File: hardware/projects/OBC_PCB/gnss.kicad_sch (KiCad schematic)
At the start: 15 parts, among them J8 RF coax pads, U1 MAX-F11N

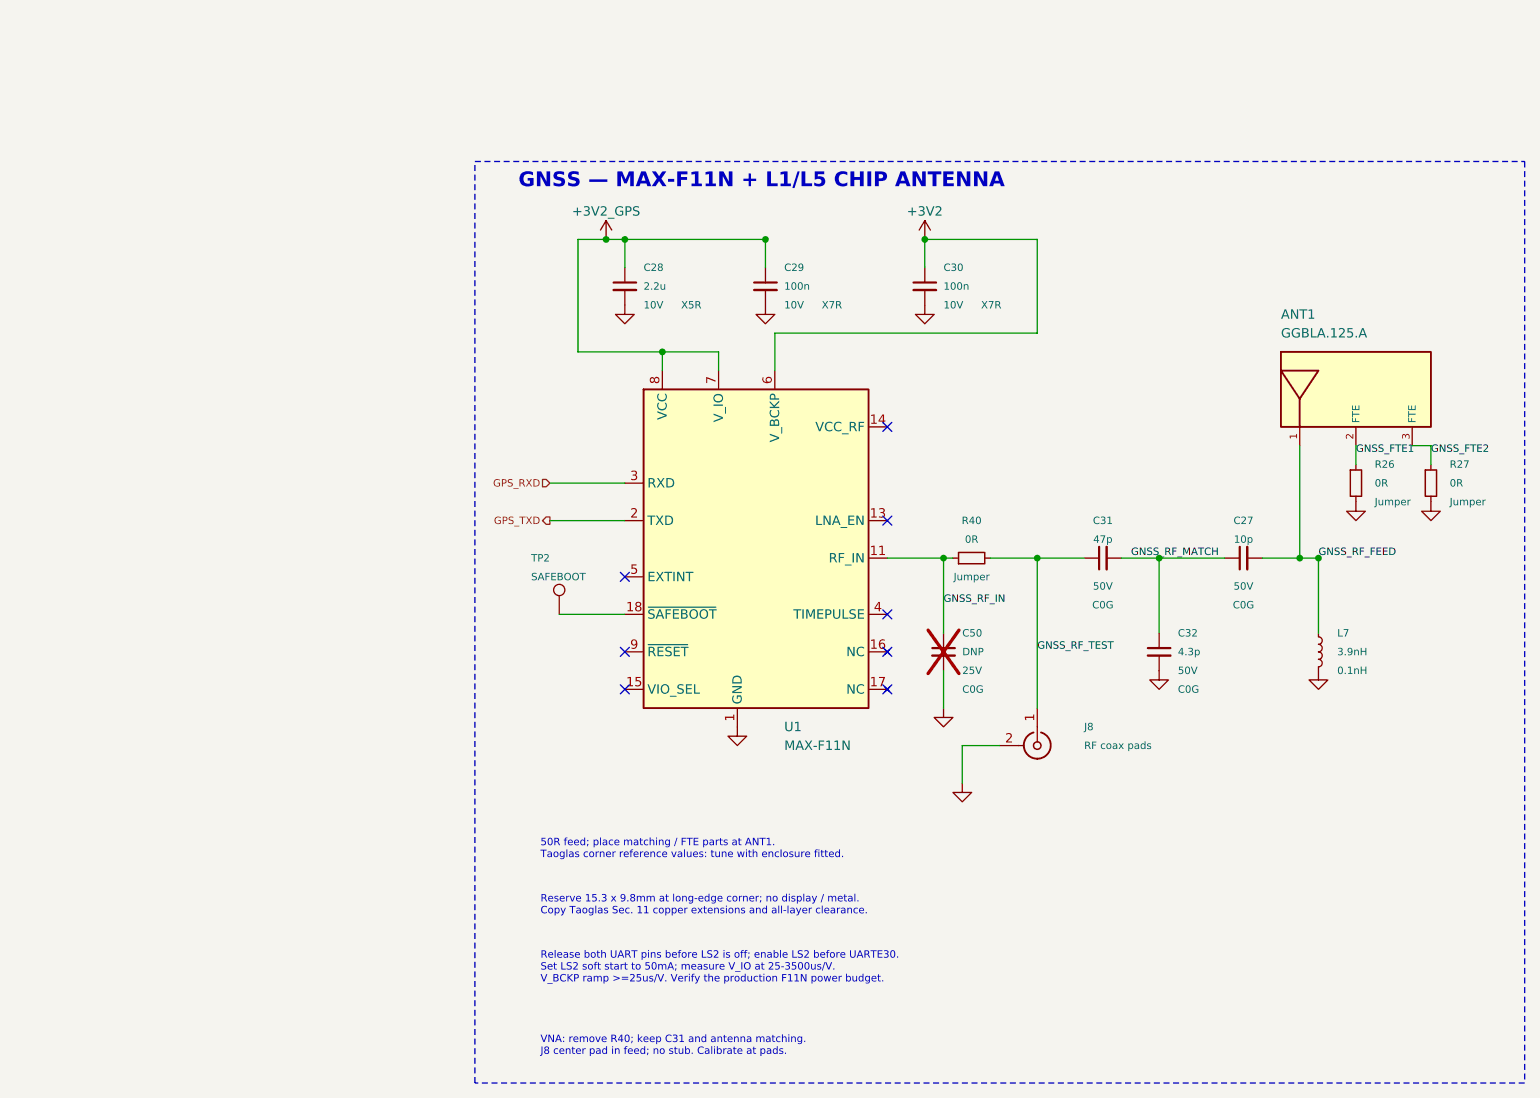
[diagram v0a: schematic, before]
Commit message: hardware: tidy the QFN schematic layout and style
Layout pass on the eight sheets. ERC stays at 0 violations on OBC_PCB and
USB_Baseboard. A netlist comparison shows the same 127 net partitions and
the same components, values and footprints.

Root sheet
- Draw SCL, SDA, COM_EN, LOUD, SHPHLD, BTN_SELECT and BUZZER_PWM as label
  stubs. Wire crossings fall from 38 to 0.
- Redraw the DCC/DECD/DECA/DECRF network as a chain without crossings.
- Move R5 and C26 clear of the crystal wires. Use a ground symbol on Y1
  instead of a label named GND.
- Hang the I2C test points on the U6C stubs.

Power sheet
- Attach the VBUS, VBAT and GND power flags to their nets.
- Tap TP1 onto the SHPHLD wire.
- Use a +3V2 symbol on LSIN2 instead of a label.
- Route SW2, the VSET straps and the CFG resistors without crossings.
- Move the SEL ground away from the LX1 pin.
- Show LSOUT1(GND) and INT(GND) for the unused LS1 and BMP581 pins.

Display, GNSS, user I/O
- Move J1 pin VA below VB so the VCOM/VB link no longer crosses VA.
- Move the GNSS FTE labels clear of the antenna pin 3 wire.
- Straighten the piezo wiring. Put the GND probe pad above its ground
  symbol.

Style
- One heading size (1.8 bold), one sub-heading size (1.27 bold) and one
  note size (1.0).
- Hide the voltage, dielectric and tolerance fields on the GNSS and radio
  sheets. Remove their dashed frames. Move both sheets to the top-left.
- Use Rev QFN and the same title format on every sheet.
- Set TP1 and TP2 to in_bom no like the other probe pads.
- Add C21 to the VDD bypass note.

Net names change for five nets because their labels are now on the root
sheet: BTN_SELECT, BUZZER_PWM, COM_EN, LOUD and SHPHLD. No net class
pattern uses them.

Co-Authored-By: Claude Sonnet 5.5 <noreply@anthropic.com>
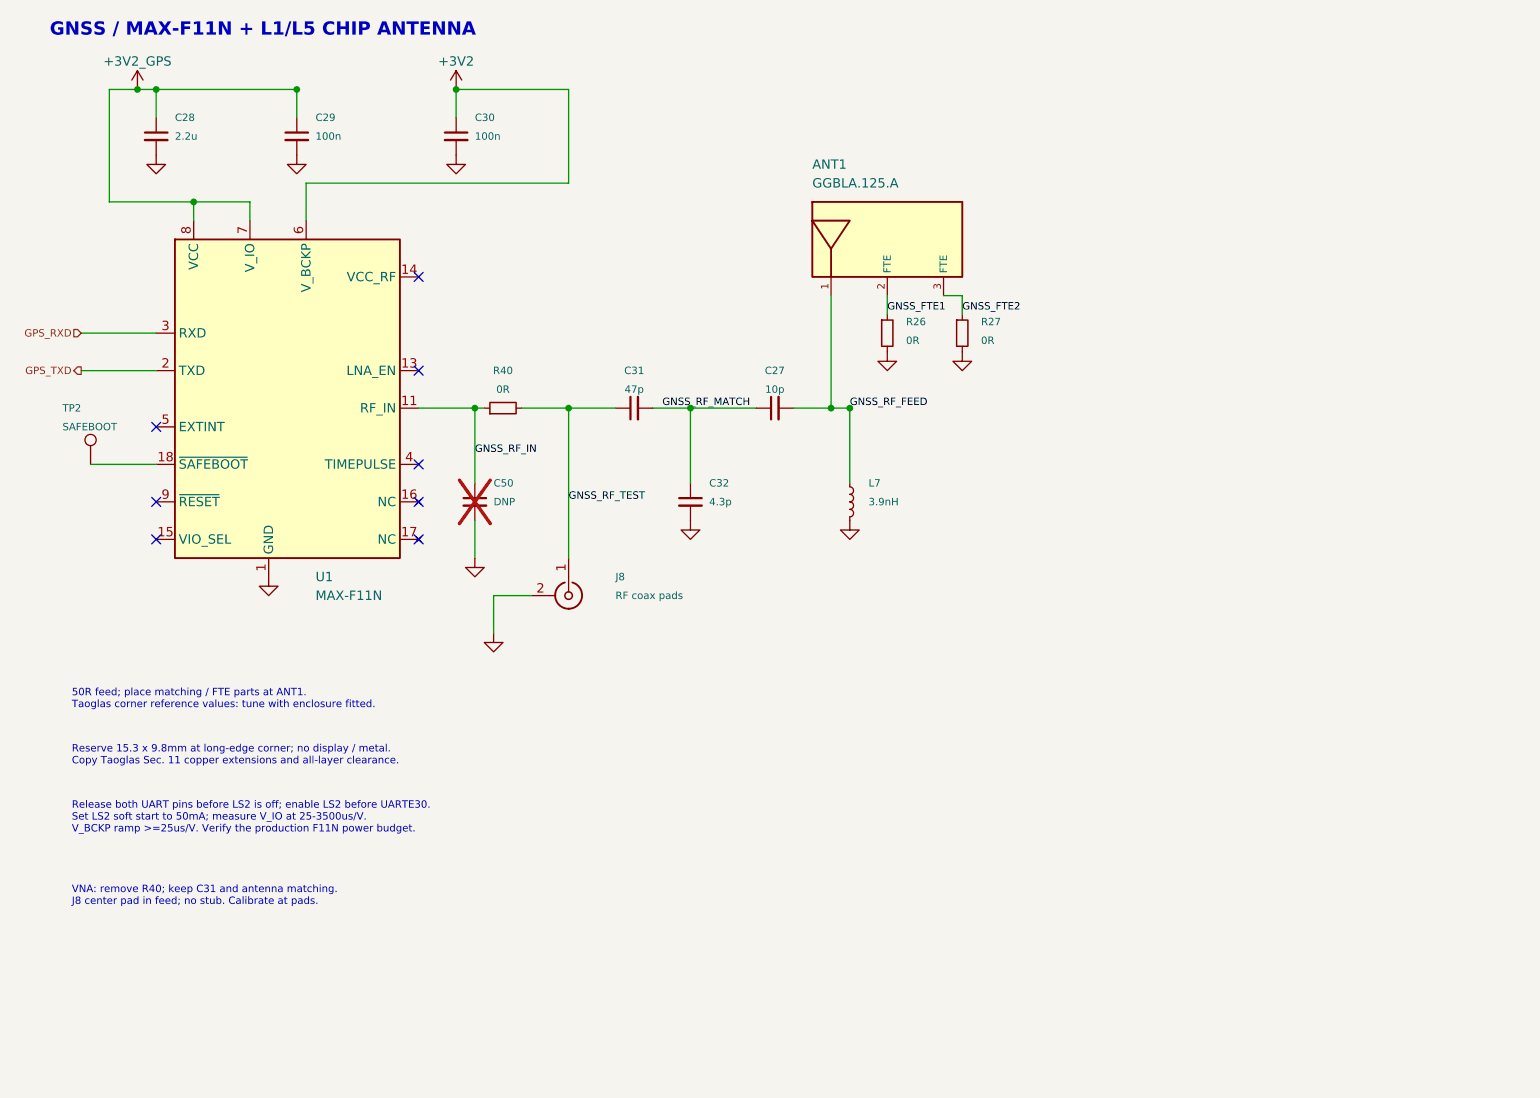
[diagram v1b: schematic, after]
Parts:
- TP2: now left out of the parts list
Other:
- note added: "GNSS / MAX-F11N + L1/L5 CHIP ANTENNA"
- note removed: "GNSS — MAX-F11N + L1/L5 CHIP ANTENNA"
- title: OpenBikeComputer — GNSS -> OpenBikeComputer - GNSS
- moved on the sheet: ANT1, C27, C28, C29, C30, C31, C32, C50, J8, L7, R26, R27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

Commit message: hardware: set the SD rail to 3.2 V, fix Y1 and tidy capacitor parts
- Power sheet note: BUCK1 runs at 3.2 V for the SD card, enabled after
  BUCK2 is at 3.2 V. C41 bias note follows. The +3V3_SD net keeps its
  name because the project net classes use it.
- Y1: CX2016DB32000D0FLJCC. It has +/-10 ppm tolerance and +/-15 ppm
  stability, 25 ppm in total against the 40 ppm Bluetooth LE limit in the
  nRF54LM20A HFXO specification. Same 2.0 x 1.6 mm package, 8 pF load.
- C47, C48 and C50 keep the dnp flag. Their value reads "tune (C0G)"
  instead of "DNP", so the BOM keeps the part class.
- C49 uses the same 2.2 uF 16 V X7R 0603 part as C39 and C40.

ERC stays at 0 violations. Only the three capacitor values change in the
netlist.

Co-Authored-By: Claude Sonnet 5.5 <noreply@anthropic.com>
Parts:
- C50: value DNP -> tune (C0G)
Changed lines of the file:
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@@
 			)
 		)
-		(property "Value" "DNP"
+		(property "Value" "tune (C0G)"
 			(at 78.74 83.82 0)
 			(show_name no)
